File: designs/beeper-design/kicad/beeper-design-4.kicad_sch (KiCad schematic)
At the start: 23 parts, among them U13 CSD75207W15, U3 BQ51003YFPR

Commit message: better export + JLCPCB numbers
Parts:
- removed C14: 2.2u, beeper-design:Pkg0201_2, symbol C318539
- removed C15: 470n, beeper-design:Pkg0402_10, symbol C106255_1
- removed C16: 470n, beeper-design:Pkg0402_4, symbol C106255
- removed C17: 22n, beeper-design:Pkg0201_21, symbol my_capacitor_5
- removed C18: 22n, beeper-design:Pkg0201_33, symbol my_capacitor_7
- removed C19: 10n, beeper-design:Pkg0201_43, symbol C272853_2
- removed C20: 10n, beeper-design:Pkg0201_6, symbol C272853
- removed C21: 270p, beeper-design:Pkg0201_19, symbol my_capacitor_3
- removed C22: 10n, beeper-design:Pkg0201_30, symbol C272853_1
- removed C23: 10u, beeper-design:Pkg0402_8, symbol C962143_4
- removed C24: 4.7u, beeper-design:Pkg0402_2, symbol C386043
- removed C25: 4.7u, beeper-design:Pkg0402, symbol C386043_1
- removed R5: 10K, beeper-design:Pkg0201, symbol C138117_2
- removed R6: 10K, beeper-design:Pkg0201_11, symbol C138117
- removed R7: 10K, beeper-design:Pkg0201_23, symbol C138117_1
- added C14: 2.2u, beeper-design:Pkg0201_41, symbol C318539_1
- added C15: 470n, beeper-design:Pkg0402_5, symbol C106255
- added C16: 470n, beeper-design:Pkg0402_10, symbol C106255_1
- added C17: 22n, beeper-design:Pkg0201_14, symbol my_capacitor_2
- added C18: 22n, beeper-design:Pkg0201_26, symbol my_capacitor_4
- added C19: 10n, beeper-design:Pkg0201_36, symbol C272853_1
- added C20: 10n, beeper-design:Pkg0201_45, symbol C272853_2
- added C21: 270p, beeper-design:Pkg0201_12, symbol my_capacitor
- added C22: 10n, beeper-design:Pkg0201_23, symbol C272853
- added C23: 10u, beeper-design:Pkg0402_3, symbol C962143_3
- added C24: 4.7u, beeper-design:Pkg0402_8, symbol C386043_1
- added C25: 4.7u, beeper-design:Pkg0402_6, symbol C386043
- added R5: 10K, beeper-design:Pkg0201_39, symbol C138117_1
- added R6: 10K, beeper-design:Pkg0201_4, symbol C138117_2
- added R7: 10K, beeper-design:Pkg0201_16, symbol C138117
- R2: footprint beeper-design:Pkg0201_13 -> beeper-design:Pkg0201_6
- R3: footprint beeper-design:Pkg0201_24 -> beeper-design:Pkg0201_17
- R4: footprint beeper-design:Pkg0201_36 -> beeper-design:Pkg0201_29
- R8: footprint beeper-design:Pkg0201_35 -> beeper-design:Pkg0201_28
- U13: footprint beeper-design:LP_7 -> beeper-design:LP_6
- U3: footprint beeper-design:LP_8 -> beeper-design:LP_7
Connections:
- net GND: now also C14.1, C23.1, C24.1, C25.1, R5.2, R6.2, R7.2
- net VBUS: now also C25.2
- net VDDSYS: now also C14.2
- net mcu_mcu-wpwr0_gpio: now also R5.1
- net mcu_mcu-wpwr1_gpio: now also R6.1
- net mcu_mcu-wpwr3_gpio: now also R7.1
- net at R4.2, U3.C2 (RECT), U3.C3 (RECT): now also C23.2, C24.2
- net at TP14.p, U3.B1 (AC2), U3.B2 (AC2): now also C16.1, C18.1, C20.1, C21.1
- net at U3.C1 (BOOT2): now also C20.2
- net at U3.B3 (AC1), U3.B4 (AC1): now also C15.1, C17.1, C19.1, C21.2, C22.2
- net at U3.E4 (COMM1): now also C17.2
- net at TP13.p: now also C22.1
- net at U3.E2 (CLAMP2): now also C16.2
- net at U3.E1 (COMM2): now also C18.2
- net at U3.C4 (BOOT1): now also C19.2
- net at U3.E3 (CLAMP1): now also C15.2

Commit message: post export, had to munge sch
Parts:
- removed C14: 2.2u, beeper-design:Pkg0201_41, symbol C318539_1
- removed C15: 470n, beeper-design:Pkg0402_5, symbol C106255
- removed C16: 470n, beeper-design:Pkg0402_10, symbol C106255_1
- removed C17: 22n, beeper-design:Pkg0201_14, symbol my_capacitor_2
- removed C18: 22n, beeper-design:Pkg0201_26, symbol my_capacitor_4
- removed C19: 10n, beeper-design:Pkg0201_36, symbol C272853_1
- removed C20: 10n, beeper-design:Pkg0201_45, symbol C272853_2
- removed C21: 270p, beeper-design:Pkg0201_12, symbol my_capacitor
- removed C22: 10n, beeper-design:Pkg0201_23, symbol C272853
- removed C23: 10u, beeper-design:Pkg0402_3, symbol C962143_3
- removed C24: 4.7u, beeper-design:Pkg0402_8, symbol C386043_1
- removed C25: 4.7u, beeper-design:Pkg0402_6, symbol C386043
- removed R2: 845R, beeper-design:Pkg0201_6, symbol my_resistor_1
- removed R3: 196R, beeper-design:Pkg0201_17, symbol C138167
- removed R4: 20K, beeper-design:Pkg0201_29, symbol C295787
- removed R5: 10K, beeper-design:Pkg0201_39, symbol C138117_1
- removed R6: 10K, beeper-design:Pkg0201_4, symbol C138117_2
- removed R7: 10K, beeper-design:Pkg0201_16, symbol C138117
- removed R8: 1K, beeper-design:Pkg0201_28, symbol C131396
- removed TP13, TP14: (no value), beeper-design:SMD_TESTPT, symbol smd_testpoint_cmp
- removed U13: CSD75207W15, beeper-design:LP_6, symbol CSD75207W15
- removed U3: BQ51003YFPR, beeper-design:LP_7, symbol BQ51003YFPR
- added C1: 22u, beeper-design:Pkg0603_2, symbol my_capacitor_12
- added C10: 2.2u, beeper-design:Pkg0201_42, symbol my_capacitor_15
- added C11: 10u, beeper-design:Pkg0402_8, symbol C105225_5
- added C12: 10u, beeper-design:Pkg0402, symbol C105225
- added C2: 22u, beeper-design:Pkg0603, symbol my_capacitor_19
- added C3: 22u, beeper-design:Pkg0603_1, symbol my_capacitor_3
- added C36: 100n, beeper-design:Pkg0201_8, symbol my_capacitor_1
- added C4: 47u, beeper-design:Pkg0805, symbol my_capacitor_6
- added C49: 1p, beeper-design:Pkg0201_16, symbol C161376
- added C5: 100n, beeper-design:Pkg0201_32, symbol my_capacitor_11
- added C50: 1p, beeper-design:Pkg0201_33, symbol C161376_1
- added C6: 47u, beeper-design:Pkg0805_1, symbol my_capacitor_17
- added C7: 10u, beeper-design:Pkg0402_1, symbol C105225_1
- added C8: 10u, beeper-design:Pkg0402_3, symbol C105225_3
- added C9: 10u, beeper-design:Pkg0402_7, symbol C105225_4
- added J1: TC2030-IDC-NL, beeper-design:TC2030_IDC_NL_FOOTPRINT, symbol component
- added J6: 10103594-0001LF, beeper-design:AMPHENOL_10103594_0001LF, symbol AMPHENOL_10103594_0001LF
- added L1: 470n, beeper-design:Pkg0201_14, symbol my_inductor
- added L2: 1u, beeper-design:Pkg0402_5, symbol C516791
- added L3: 1n, beeper-design:Pkg0201_24, symbol my_inductor_1
- added L4: 1n, beeper-design:Pkg0201_41, symbol my_inductor_2
- added R1: 0R, beeper-design:Pkg0201_4, symbol my_resistor_1
- added R18: 100K, beeper-design:Pkg0201_44, symbol my_resistor_11
- added TP10, TP11, TP12, TP5, TP6, TP7, TP8, TP9: (no value), beeper-design:SMD_TESTPT, symbol smd_testpoint_cmp
- added U1: DA14705-00000HZ2, beeper-design:LP, symbol DA14705
- added U17: (no value), beeper-design:Pkg_2450AT18D0100_STD_R_1, symbol Sym2450AT18D0100
- added U7: TPD4S012DRYR, beeper-design:SON_6_L1_5_W1_0_P0_50_BL, symbol C96506
- added XTAL1: XRCGB32M000F1H00R0, beeper-design:CRYSTAL_SMD_4P_L2_0_W1_6_BL_1, symbol C880116
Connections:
- net GND: now also C1.1, C10.1, C11.1, C12.1, C2.1, C3.1, C36.2, C4.1, C49.2, C5.1, C50.2, C6.1, C7.1, C8.1, C9.1, J1.5, J6.5 (GND), R18.2, TP10.p, TP12.p, U1.A11 (RFIOM2), U1.A12 (PSUBRF), U1.A8 (PSUB), U1.A9 (RFIOM1), U1.B9 (ESDN), U1.C12 (GND_RF2), U1.C2 (VSSIOQQ), U1.D12 (GND_RF1), U1.E11 (GND_XTAL2), U1.E12 (GND_XTAL1), U1.F5 (VSSD4), U1.F6 (VSSD3), U1.G12 (GND_XTAL3), U1.G5 (VSSD1), U1.G6 (VSSD2), U1.G7 (VSSD5), U1.H1 (GND_BOOST), U1.H6 (AVS1), U1.H7 (AVS2), U1.H8 (AVS3), U1.L8 (GND_SDADC), U1.L9 (GND_VAD), U1.M1 (GND_BUCK), U17.2 (GND), U17.3 (GND), U17.4 (GND), U7.4 (GND), XTAL1.2 (GND1), XTAL1.4 (GND0)
- net VBUS: now also J6.1 (VCC), U7.6 (VBUS)
- net mcu_mcu-wpwr0_gpio: now also U1.J4 (P1_09)
- net mcu_mcu-wpwr1_gpio: now also U1.K4 (P1_00)
- net mcu_mcu-wpwr2_gpio: now also U1.K3 (P1_07)
- net mcu_mcu-wpwr3_gpio: now also U1.J5 (P1_25)
- new net: L1.1, U1.M2 (LX)
- new net: L1.2, U1.L1 (LY)
- new net: C6.2, R1.2, U1.J2 (V18P)
- new net: C9.2, U1.M5 (VBUS)
- new net: J1.2, U1.C7 (P0_00)
- new net: J1.4, U1.D6 (P0_01)
- new net: J1.3, U1.G8 (P0_16)
- new net: J1.6, U1.G9 (P0_10)
- new net: TP5.p, U1.K5 (P0_31)
- new net: C5.2, R1.1, U1.C1 (V18F)
- new net: C2.2, C3.2, U1.A7 (V14RF), U1.L2 (V14)
- new net: U1.F11 (XTAL32Mp), XTAL1.1
- new net: U1.F12 (XTAL32Mm), XTAL1.3
- new net: C36.1, J6.10 (SHIELD), J6.11 (SHIELD), J6.13 (SHIELD), J6.14 (SHIELD), J6.6 (SHIELD), J6.7 (SHIELD), J6.8 (SHIELD), J6.9 (SHIELD), R18.1
- new net: L2.1, U1.J1 (LZ)
- new net: C1.2, U1.L3 (V12)
- new net: C8.2, TP11.p, U1.M4 (VBAT)
- new net: TP7.p, U1.K7 (P1_22)
- new net: TP8.p, U1.J7 (P1_31)
- new net: TP6.p, U1.J8 (P1_30)
- new net: TP9.p, U1.K6 (P1_23)
- new net: U1.J10 (NC), U1.J11 (NC), U1.J12 (NC), U1.K10 (NC), U1.K11 (NC), U1.K12 (NC), U1.L10 (NC), U1.L11 (NC), U1.L12 (NC), U1.M10 (NC), U1.M11 (NC), U1.M12 (NC)
- new net D+: J6.3 (D+), U1.F1 (P2_10), U7.1 (D+)
- new net D-: J6.2 (D-), U1.G1 (P2_11), U7.2 (D-)
- new net RF1: C49.1, L3.1, U1.A10 (RFIOP)
- new net RF2: C50.1, L3.2, L4.1
- new net RF3: L4.2, U17.1 (ANT)
- new net VDD1P8: C11.2, C12.2, C4.2, J1.1, L2.2, U1.K2 (V18), U1.M3 (VSYS)
- new net VDD3P0: C7.2, U1.M6 (V30)
- new net VLED: C10.2, U1.K1 (VLED)
- new net board-io_qsen-i3c_scl: U1.K9 (P1_12)
- new net board-io_qsen-i3c_sda: U1.K8 (P1_11)
- new net board-io_rgb_b: U1.L4 (LED3)
- new net board-io_rgb_g: U1.L6 (LED2)
- new net board-io_rgb_r: U1.L5 (LED1)
- new net codec-i2c-net_scl: U1.B1 (P2_04)
- new net codec-i2c-net_sda: U1.H2 (P0_22)
- new net mcu_hap-gpio0_gpio: U1.J9 (P2_01)
- new net mcu_hap-gpio1_gpio: U1.H9 (P0_23)
- new net mcu_hap-i2c_scl: U1.G10 (P0_08)
- new net mcu_hap-i2c_sda: U1.M7 (P1_05)
- new net mcu_mcu-button0_gpio: U1.D11 (P0_28)
- new net mcu_mcu-button1_gpio: U1.M8 (P1_06)
- new net mcu_mcu-button2_gpio: U1.H3 (P1_26)
- new net mcu_mcu-mem_cs: U1.J3 (P1_24)
- new net mcu_mcu-mem_sck: U1.F4 (P1_19)
- new net mcu_mcu-mem_sdio0: U1.J6 (P1_15)
- new net mcu_mcu-mem_sdio1: U1.G2 (P1_14)
- new net mcu_mcu-mem_sdio2: U1.H4 (P1_13)
- new net mcu_mcu-mem_sdio3: U1.F3 (P1_20)
- new net mcu_q-spi_cs: U1.H11 (P2_09)
- new net mcu_q-spi_sck: U1.H12 (P2_08)
- new net mcu_q-spi_sdi: U1.H10 (P0_30)
- new net mcu_q-spi_sdo: U1.L7 (P0_27)
- no-connect marks 0 -> 1

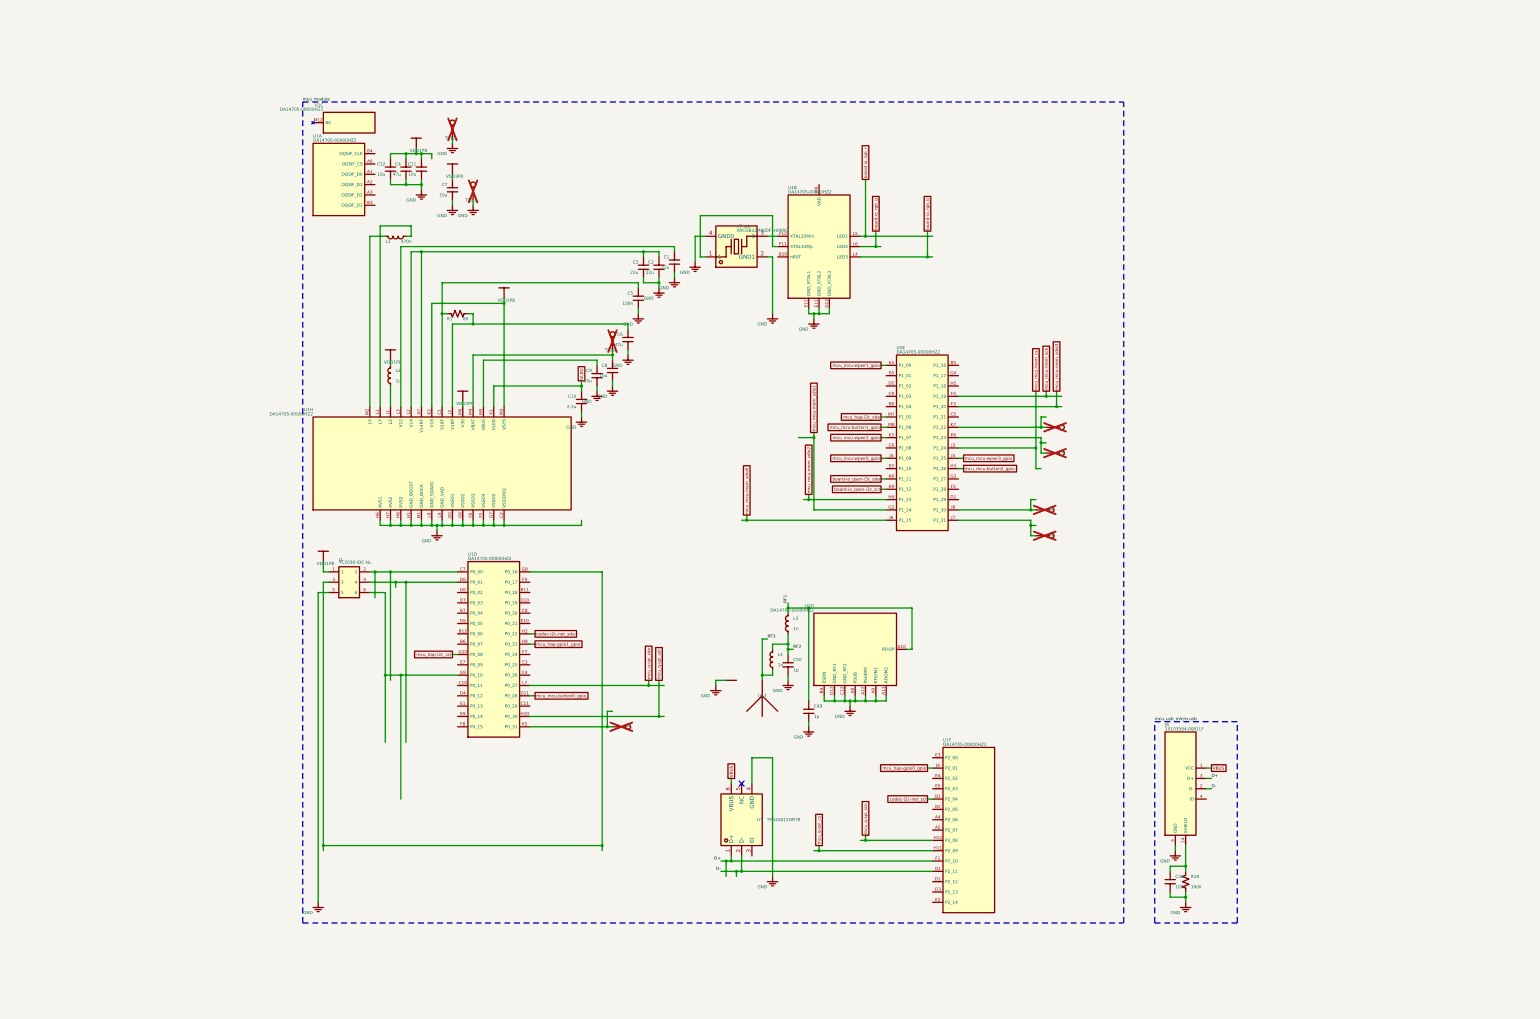
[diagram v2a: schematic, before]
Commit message: fixing drc errors
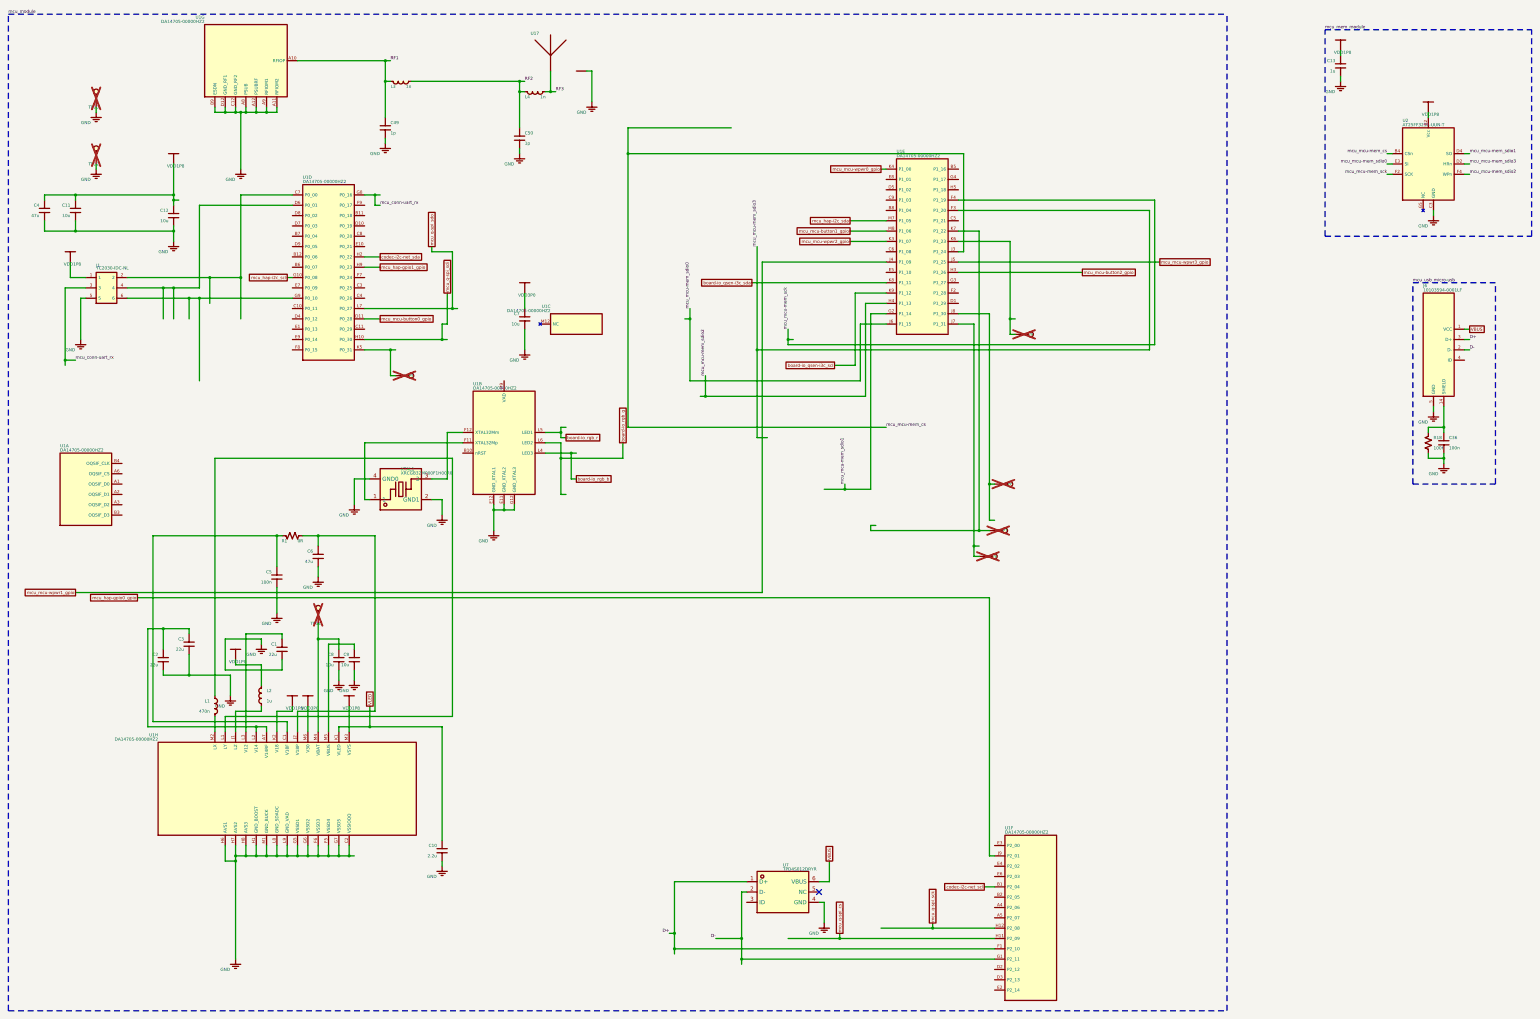
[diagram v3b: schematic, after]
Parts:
- added C13: 1u, beeper-design:Pkg0201_10, symbol C76935_3
- added U2: AT25FF321A-UUN-T, beeper-design:WLCSP_12, symbol AT25FF321A_UUN_T
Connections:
- net GND: now also C13.1, U2.C3 (GND)
- net VDD1P8: now also C13.2, U2.B2 (Vcc)
- net mcu_mcu-mem_cs: now also U2.B4 (CSn)
- net mcu_mcu-mem_sck: now also U2.F2 (SCK)
- net mcu_mcu-mem_sdio0: now also U2.E3 (SI)
- net mcu_mcu-mem_sdio1: now also U2.D4 (SO)
- net mcu_mcu-mem_sdio2: now also U2.F4 (WPn)
- net mcu_mcu-mem_sdio3: now also U2.D2 (HRn)
- net mcu_mcu-wpwr0_gpio: now also U1.K4 (P1_00); no longer U1.J4 (P1_09)
- net mcu_mcu-wpwr1_gpio: now also U1.J4 (P1_09); no longer U1.K4 (P1_00)
- net mcu_conn-uart_rx: now reaches J1.3, U1.G8 (P0_16)
- new net: U2.A1 (NC), U2.A5 (NC), U2.G1 (NC), U2.G5 (NC)

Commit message: made ocdb a submodule
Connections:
- net VDD1P8 renamed VDDSYS

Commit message: kicad exported data
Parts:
- removed C1: 22u, beeper-design:Pkg0603_2, symbol my_capacitor_12
- removed C10: 2.2u, beeper-design:Pkg0201_42, symbol my_capacitor_15
- removed C11: 10u, beeper-design:Pkg0402_8, symbol C105225_5
- removed C12: 10u, beeper-design:Pkg0402, symbol C105225
- removed C13: 1u, beeper-design:Pkg0201_10, symbol C76935_3
- removed C2: 22u, beeper-design:Pkg0603, symbol my_capacitor_19
- removed C3: 22u, beeper-design:Pkg0603_1, symbol my_capacitor_3
- removed C36: 100n, beeper-design:Pkg0201_8, symbol my_capacitor_1
- removed C4: 47u, beeper-design:Pkg0805, symbol my_capacitor_6
- removed C49: 1p, beeper-design:Pkg0201_16, symbol C161376
- removed C5: 100n, beeper-design:Pkg0201_32, symbol my_capacitor_11
- removed C50: 1p, beeper-design:Pkg0201_33, symbol C161376_1
- removed C6: 47u, beeper-design:Pkg0805_1, symbol my_capacitor_17
- removed C7: 10u, beeper-design:Pkg0402_1, symbol C105225_1
- removed C8: 10u, beeper-design:Pkg0402_3, symbol C105225_3
- removed C9: 10u, beeper-design:Pkg0402_7, symbol C105225_4
- removed J1: TC2030-IDC-NL, beeper-design:TC2030_IDC_NL_FOOTPRINT, symbol component
- removed L1: 470n, beeper-design:Pkg0201_14, symbol my_inductor
- removed L2: 1u, beeper-design:Pkg0402_5, symbol C516791
- removed L3: 1n, beeper-design:Pkg0201_24, symbol my_inductor_1
- removed R1: 0R, beeper-design:Pkg0201_4, symbol my_resistor_1
- removed R18: 100K, beeper-design:Pkg0201_44, symbol my_resistor_11
- removed U17: (no value), beeper-design:Pkg_2450AT18D0100_STD_R_1, symbol Sym2450AT18D0100
- added C1: 22u, beeper-design:Pkg0603, symbol C86295
- added C10: 2.2u, beeper-design:Pkg0201_37, symbol C335106_24
- added C11: 2.2u, beeper-design:Pkg0201_29, symbol C335106_19
- added C12: 2.2u, beeper-design:Pkg0201_48, symbol C335106_30
- added C13: 2.2u, beeper-design:Pkg0201_51, symbol C335106_33
- added C2: 22u, beeper-design:Pkg0603_1, symbol C86295_1
- added C3: 22u, beeper-design:Pkg0603_2, symbol C86295_2
- added C36: 2.2u, beeper-design:Pkg0201_49, symbol C335106_31
- added C4: 47u, beeper-design:Pkg0805, symbol my_capacitor
- added C49: 2.2u, beeper-design:Pkg0201_4, symbol C335106_1
- added C5: 2.2u, beeper-design:Pkg0201_24, symbol C335106_14
- added C50: 2.2u, beeper-design:Pkg0201_25, symbol C335106_15
- added C6: 47u, beeper-design:Pkg0805_1, symbol my_capacitor_1
- added C7: 2.2u, beeper-design:Pkg0201_50, symbol C335106_32
- added C8: 2.2u, beeper-design:Pkg0201_6, symbol C335106_2
- added C9: 2.2u, beeper-design:Pkg0201_22, symbol C335106_12
- added J1: TC2030-IDC-NL, beeper-design:TC2030_IDC_NL_FOOTPRINT, symbol component_1
- added L1: 470n, beeper-design:Pkg0201_1, symbol my_inductor_3
- added L2: 470n, beeper-design:Pkg0201_14, symbol my_inductor_1
- added L3: 470n, beeper-design:Pkg0201_13, symbol my_inductor
- added R1: 0R, beeper-design:Pkg0201_44, symbol my_resistor_11
- added R18: 100K, beeper-design:Pkg0201_38, symbol my_resistor_8
- added U17: (no value), beeper-design:Pkg_2450AT18D0100_STD_R_1, symbol Sym2450AT18D0100001E
- L4: value 1n -> 470n; footprint beeper-design:Pkg0201_41 -> beeper-design:Pkg0201_36; MPN BSCQ000603031N0B00 -> LQP03HQR47H02D; Manufacturer Chilisin Electronics -> MURATA
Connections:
- net GND: now also C1.1, C10.1, C11.1, C12.1, C13.1, C2.1, C3.1, C36.2, C4.1, C49.2, C5.1, C50.2, C6.1, C7.1, C8.1, C9.1, J1.5, R18.2, U17.2 (GND), U17.3 (GND), U17.4 (GND)
- net RF1: now also C49.1, L3.1
- net RF2: now also C50.1, L3.2
- net RF3: now also U17.1 (ANT)
- net VDD3P0: now also C7.2
- net VLED: now also C10.2
- net SHIELD: now reaches J6.10 (SHIELD), J6.11 (SHIELD), J6.13 (SHIELD), J6.14 (SHIELD), J6.6 (SHIELD), J6.7 (SHIELD), J6.8 (SHIELD), J6.9 (SHIELD)
- net SHIELD: now also C36.1, R18.1
- net at TP11.p, U1.M4 (VBAT): now also C8.2
- net at U1.C1 (V18F): now also C5.2, R1.1
- net at U1.A7 (V14RF), U1.L2 (V14): now also C2.2, C3.2
- net at U1.J1 (LZ): now also L2.1
- net at U1.J2 (V18P): now also C6.2, R1.2
- net at U1.L1 (LY): now also L1.2
- net at U1.L3 (V12): now also C1.2
- net at U1.M2 (LX): now also L1.1
- net at U1.M5 (VBUS): now also C9.2
- net at U1.C7 (P0_00): now also J1.2
- net at U1.D6 (P0_01): now also J1.4
- net at U1.G9 (P0_10): now also J1.6
- net VDDSYS renamed VDD1P8
- net VDD1P8: now also C11.2, C12.2, C13.2, C4.2, J1.1, L2.2
- net board-io_qsen-i3c_sda renamed mcu_q-i3c_sda
- net mcu_conn-uart_rx renamed mcu_mcu-uart_rx
- net mcu_mcu-uart_rx: now also J1.3
